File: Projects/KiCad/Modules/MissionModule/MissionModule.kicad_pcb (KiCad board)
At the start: 2 copper layers, 110 x 95 mm, 55 parts, among them J1 Conn_01x08, J2 Micro_SD_Card_Det_Hirose_DM3AT, SW1 SW_DIP_x02, U1 MCP2562-E-P, U2 MCP2515-I/P, U3 NJM7805SDL1, U5 TLP222A, U6 ABX00012, U7 MB85RS2MT, U8 MB85RS2MT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

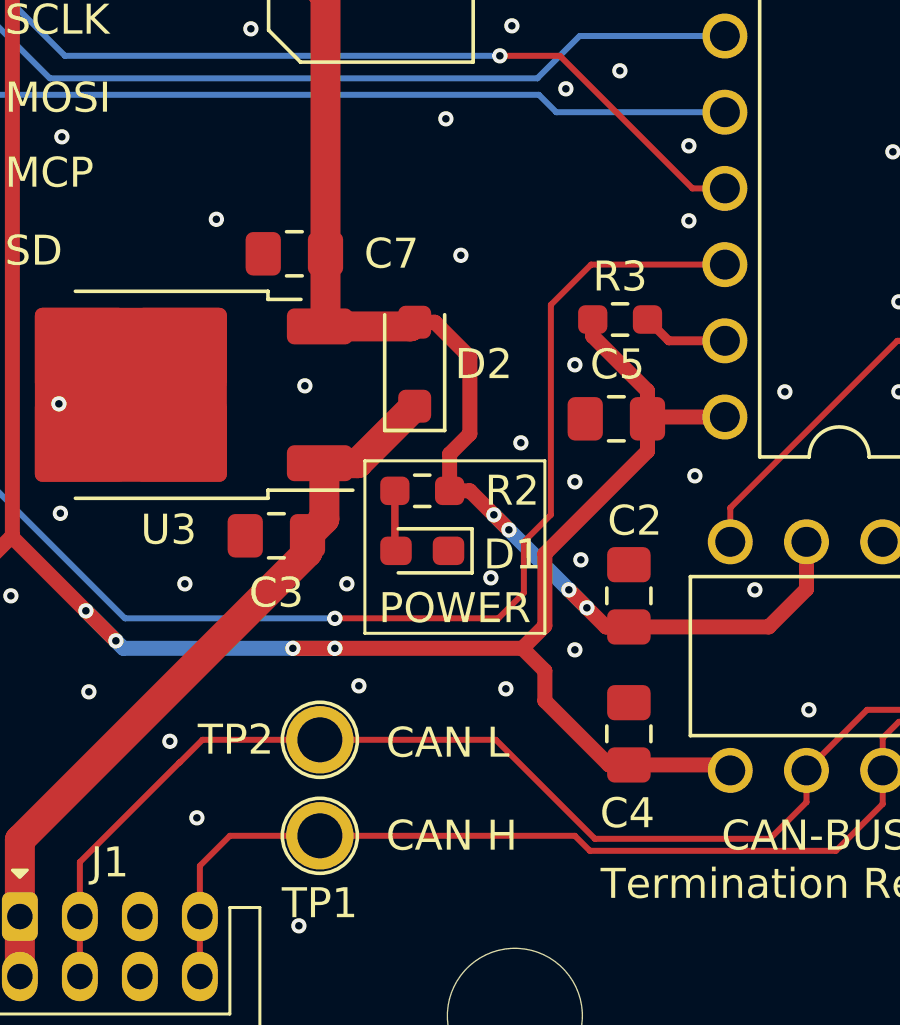
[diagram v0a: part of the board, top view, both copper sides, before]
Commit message: チップ積層セラミックコンデンサをSMD1608に変更
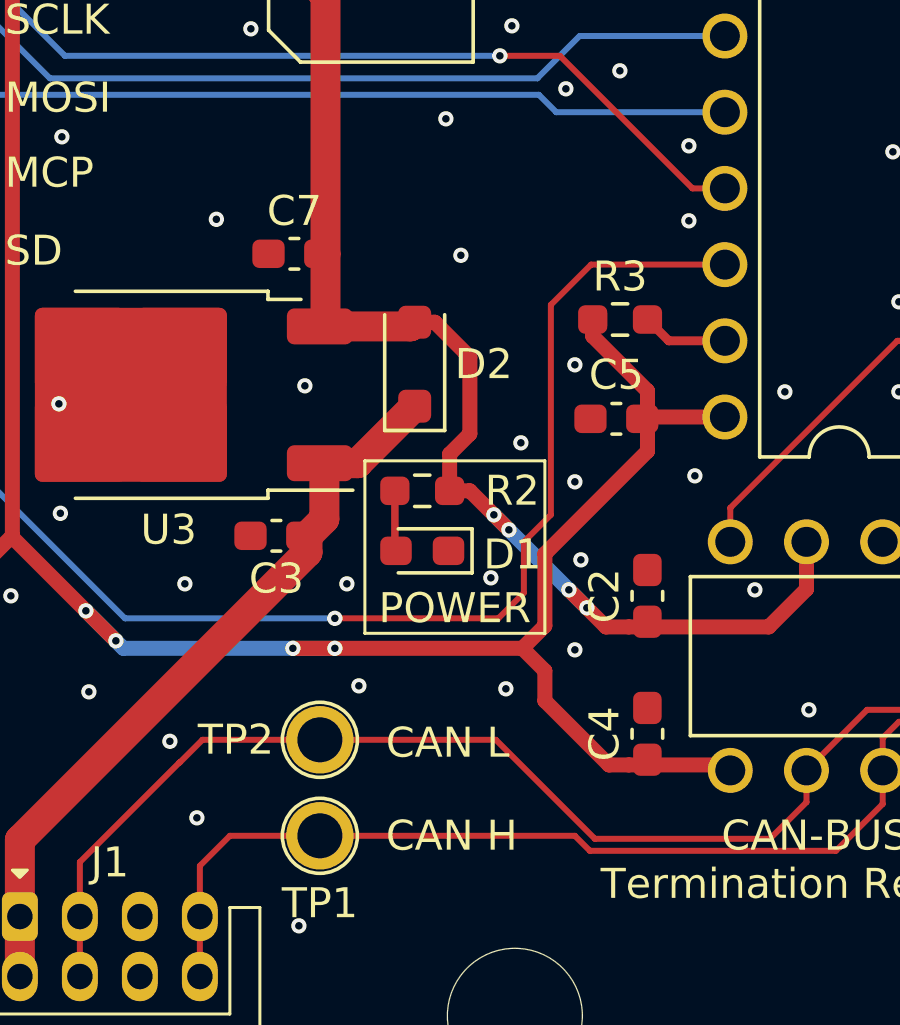
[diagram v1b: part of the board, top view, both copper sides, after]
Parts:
- C2, C3, C4, C5, C7: footprint Capacitor_SMD:C_0805_2012Metric_Pad1.18x1.45mm_HandSolder -> Capacitor_SMD:C_0603_1608Metric_Pad1.08x0.95mm_HandSolder
- moved C2 0.62 mm to (182.9, 121.0)
- moved C4 0.62 mm to (182.9, 125.6)

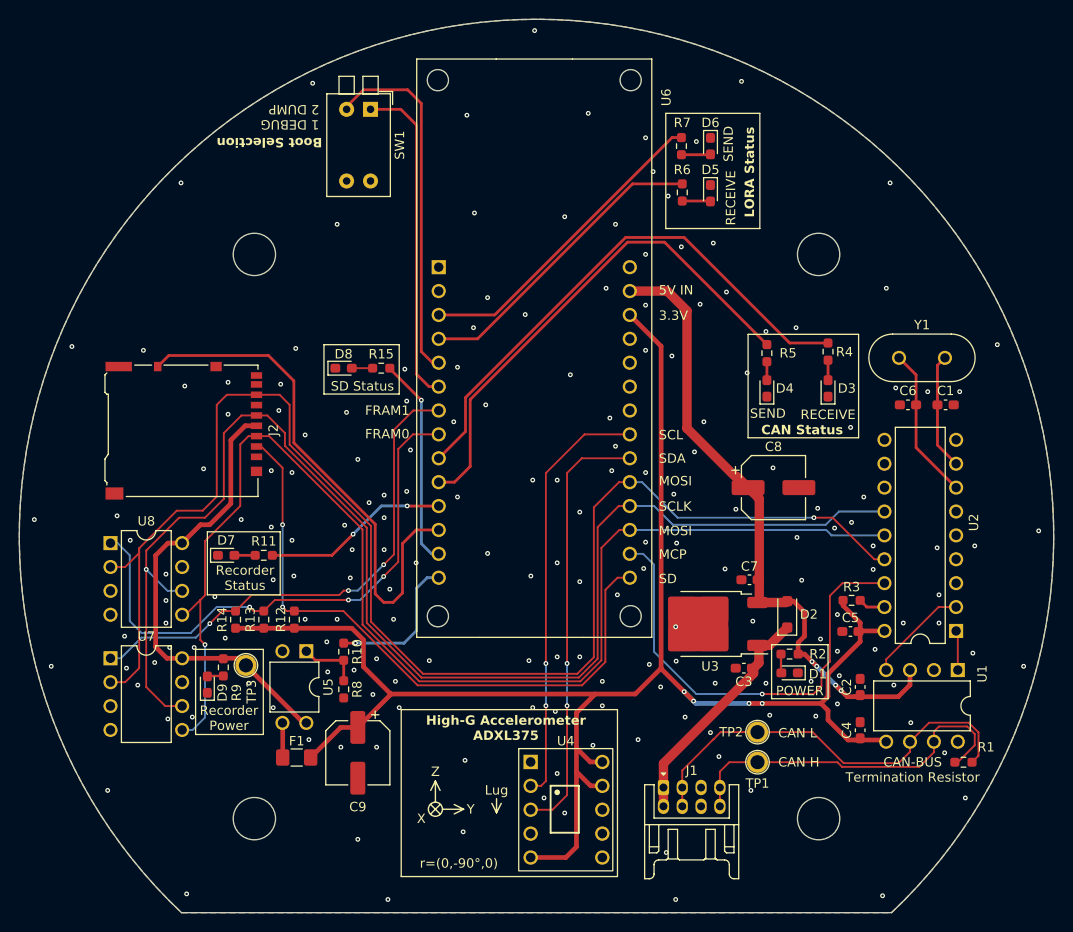
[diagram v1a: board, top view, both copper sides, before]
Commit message: 抵抗の在庫に合わせてサイズを変更
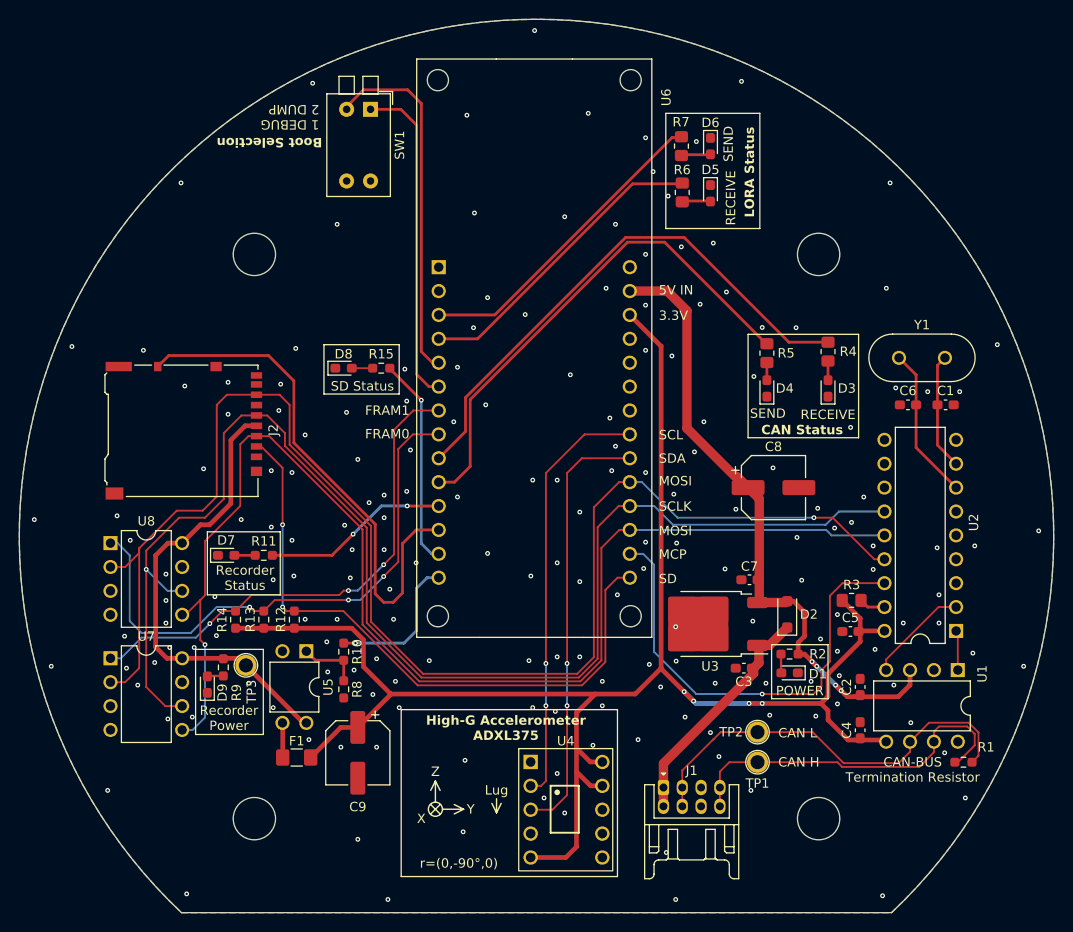
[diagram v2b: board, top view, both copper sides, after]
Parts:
- R3, R4, R5, R6, R7: footprint Resistor_SMD:R_0603_1608Metric_Pad0.98x0.95mm_HandSolder -> Resistor_SMD:R_0805_2012Metric_Pad1.20x1.40mm_HandSolder

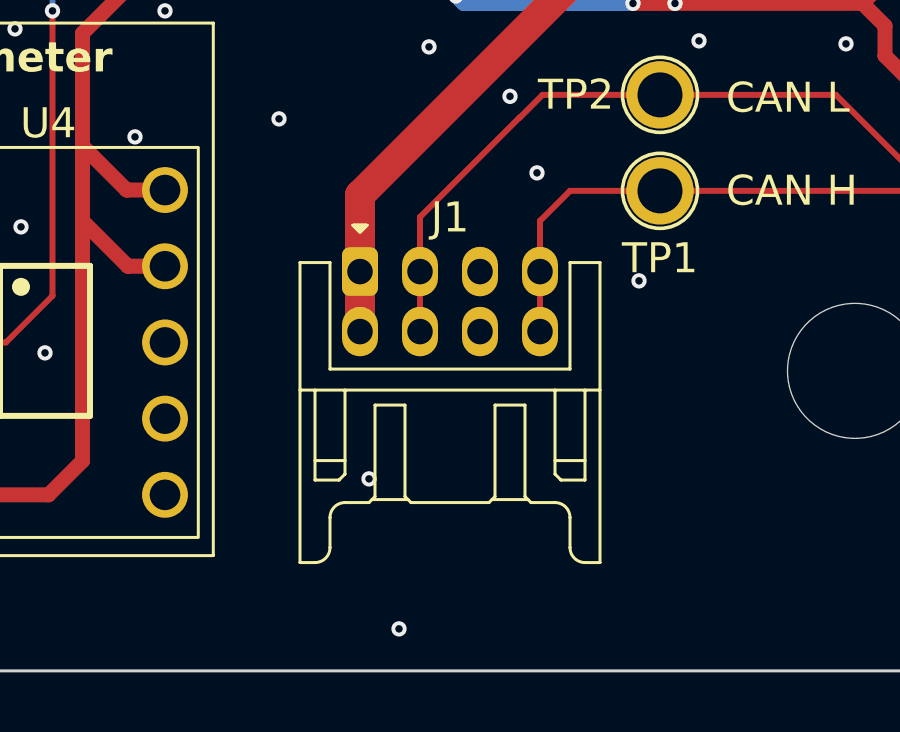
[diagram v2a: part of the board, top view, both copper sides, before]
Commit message: コネクタ位置を揃えた
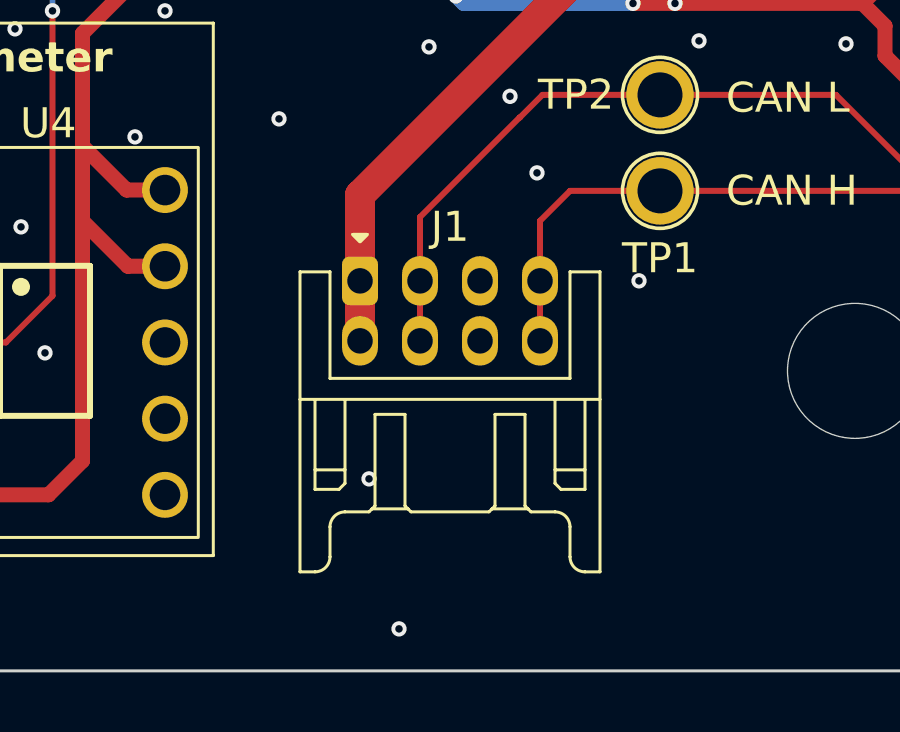
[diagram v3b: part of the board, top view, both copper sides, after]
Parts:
- moved J1 0.31 mm to (162.0, 132.0)

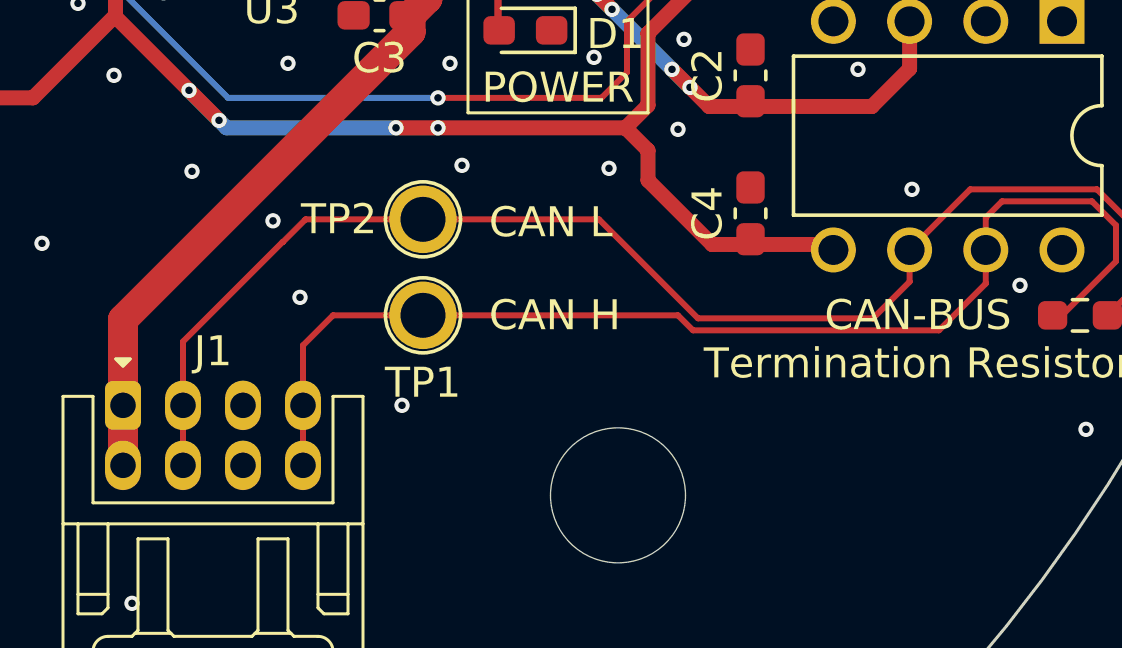
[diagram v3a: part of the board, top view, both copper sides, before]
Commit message: コネクタのピン配置を変更
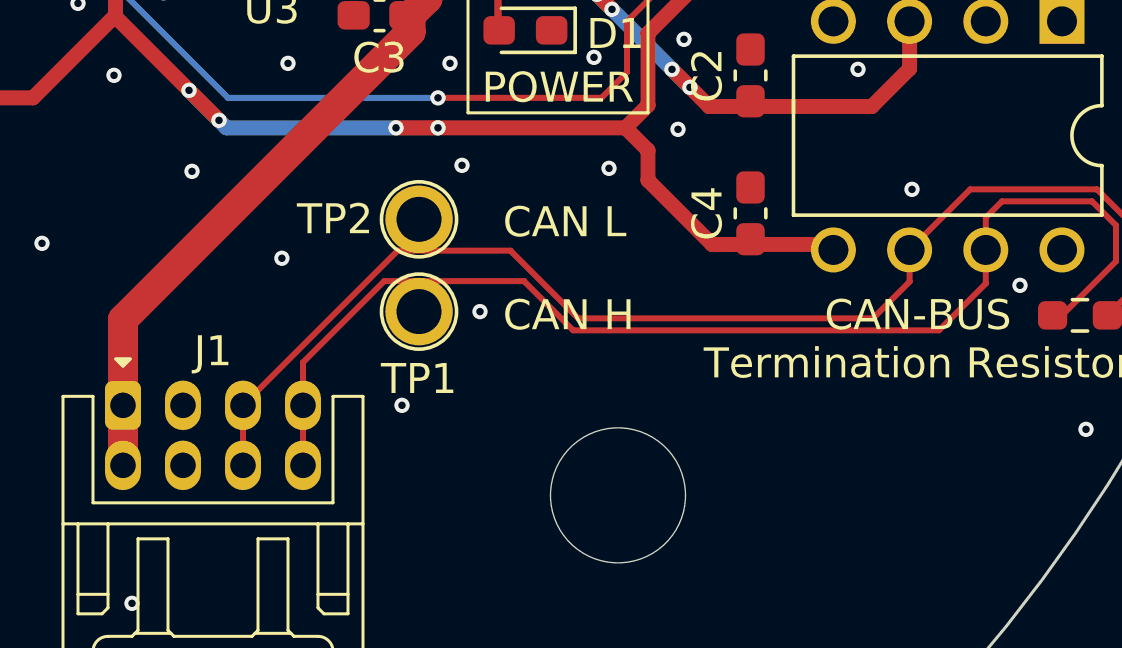
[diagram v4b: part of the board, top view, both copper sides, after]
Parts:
- C3: value 0.33μF -> 10μF
- moved TP1 0.18 mm to (171.9, 128.9)
- moved TP2 0.13 mm to (171.9, 125.8)
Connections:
- J1 pad 3: CAN_L -> GND
- J1 pad 4: CAN_L -> GND
- J1 pad 5: GND -> CAN_L
- J1 pad 6: GND -> CAN_L
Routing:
- net CAN_L: track 45.0 -> 40.9 mm
- net CAN_H: track 38.9 -> 39.5 mm

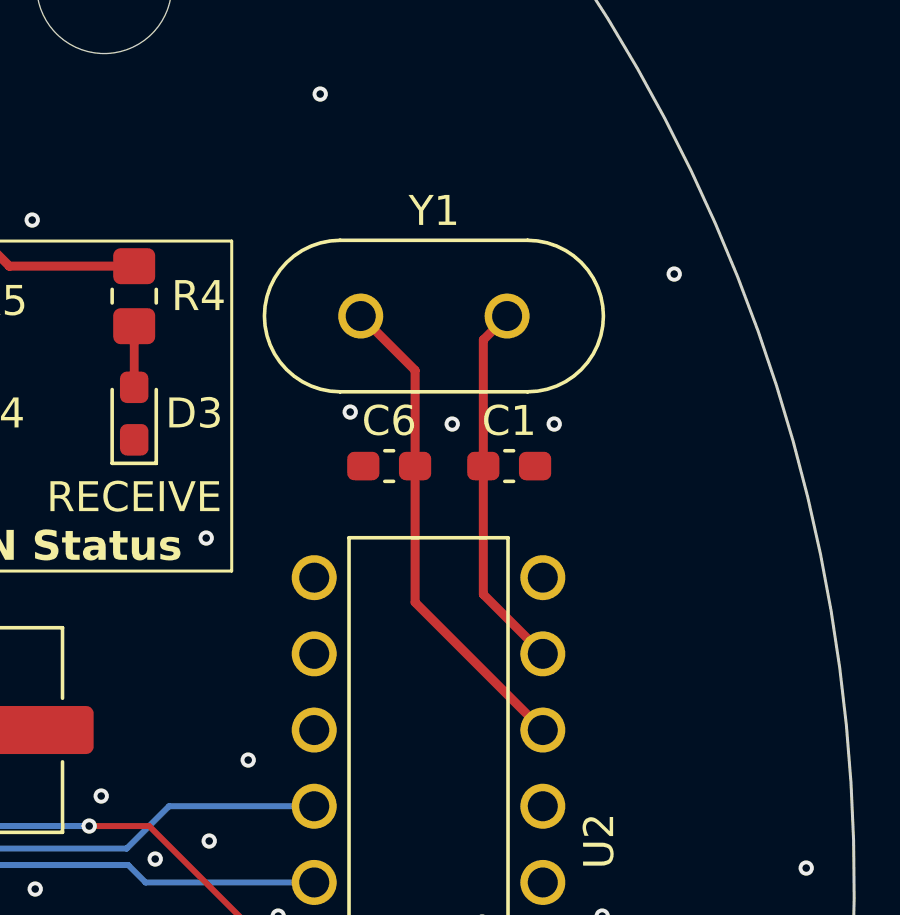
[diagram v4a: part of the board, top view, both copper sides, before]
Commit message: クリスタルをSMDに変更
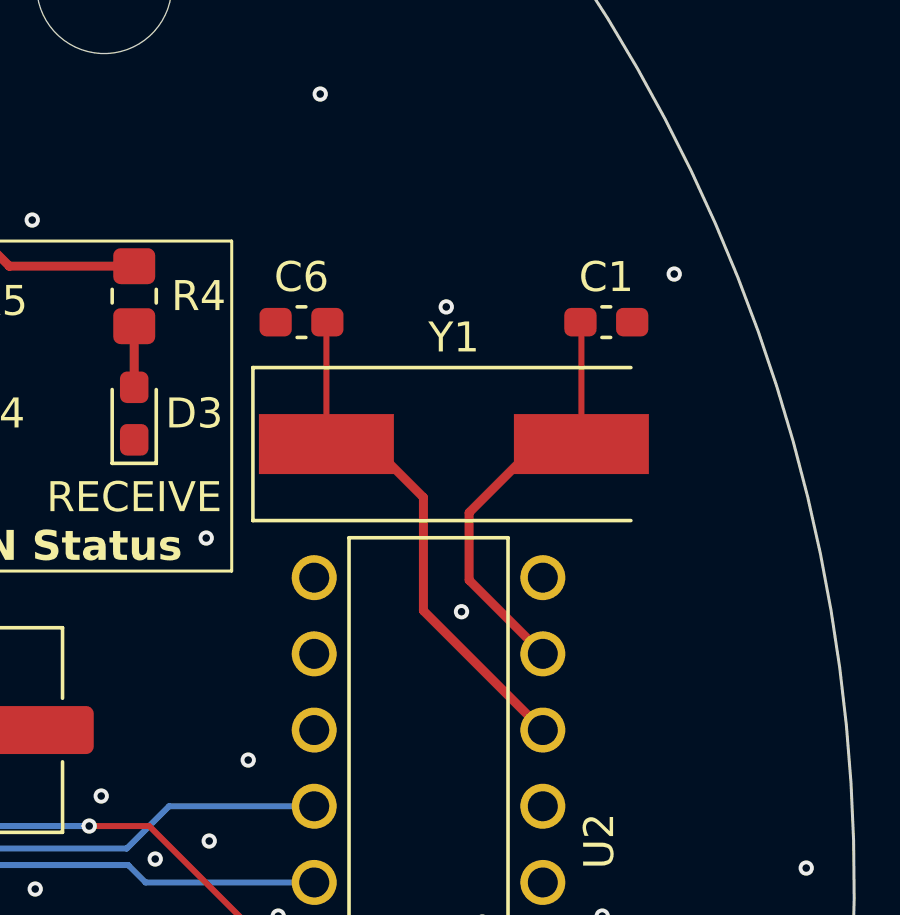
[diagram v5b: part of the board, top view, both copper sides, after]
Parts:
- Y1: footprint Crystal:Crystal_HC49-U_Vertical -> Crystal:Crystal_SMD_HC49-SD
- moved C1 5.79 mm to (195.2, 86.2)
- moved C6 5.62 mm to (185.1, 86.2)
- moved Y1 5.28 mm to (190.2, 90.3)
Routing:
- net OSC1: track 12.4 -> 14.5 mm
- net OSC2: track 16.3 -> 17.5 mm
- net GND: vias 188 -> 187
